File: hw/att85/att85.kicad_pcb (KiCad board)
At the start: 2 copper layers, 80 x 40 mm, 41 parts, among them J101 Barrel_Jack_Switch, J102 Screw_Terminal_01x03, J103 AVR-ISP-6, J104 Conn_01x02, Q101 BC817, SW101 SW_Push, SW102 SW_Push, SW103 SW_Push, SW104 SW_Push, SW105 SW_Push, SW106 SW_Push, U101 ATtiny85-20P, U102 MT3608-MODULE, U103 VS1838B

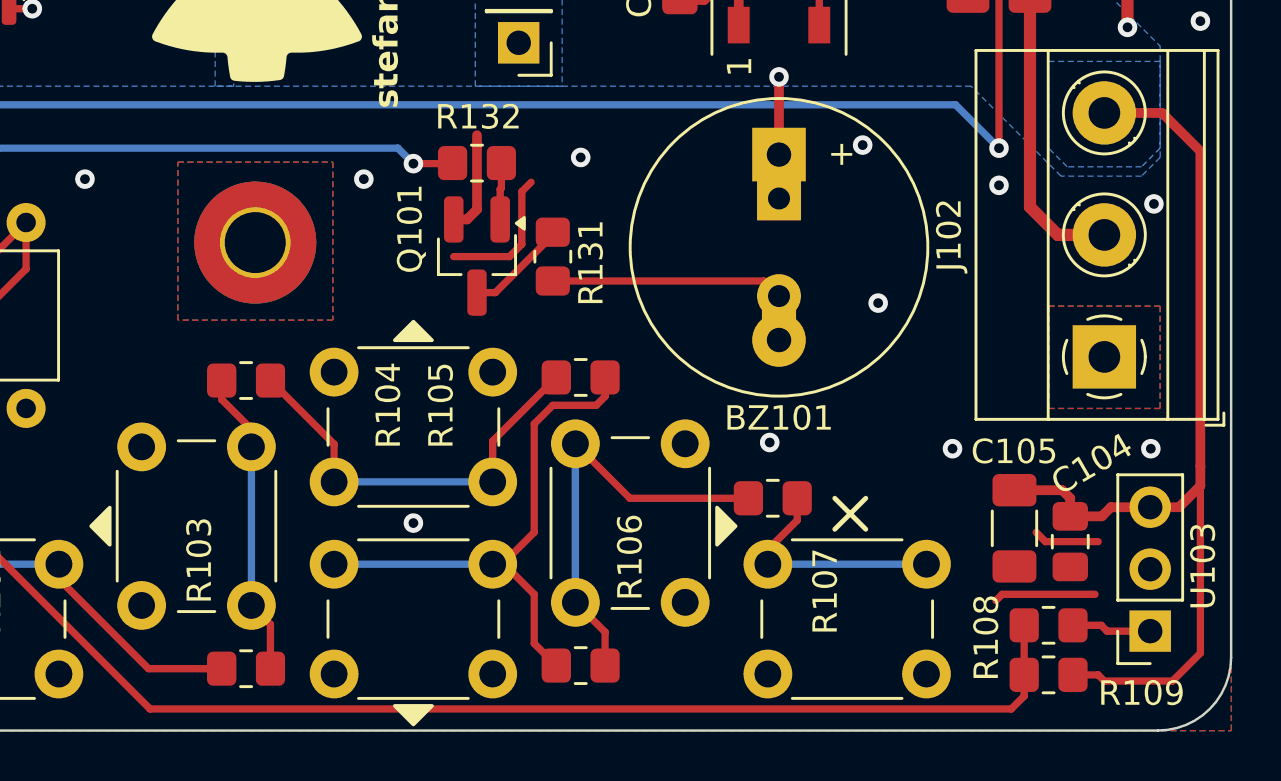
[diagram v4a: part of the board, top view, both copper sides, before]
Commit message: fix(hw): move IR receiver resistor according the datasheet
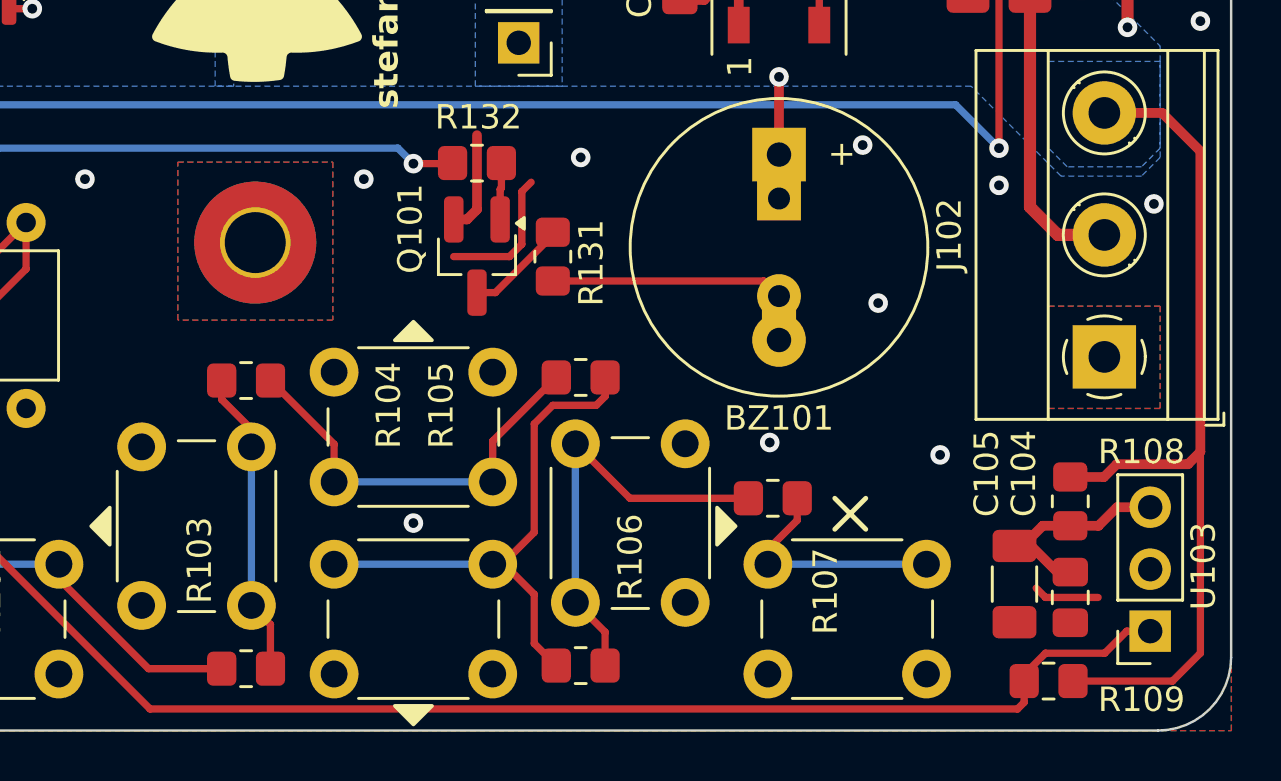
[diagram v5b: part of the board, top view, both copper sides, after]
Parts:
- moved R108 5.16 mm to (192.8, 105.5), turned to 90 degrees
- moved C104 2.29 mm to (192.8, 109.5)
- moved C105 2.29 mm to (190.5, 108.9)
- moved R109 0.25 mm to (191.9, 112.9)
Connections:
- C104 pad 1: +5V -> Net-(U103-VCC)
- C105 pad 1: +5V -> Net-(U103-VCC)
- R108 pad 1: /IR/MOSI -> Net-(U103-VCC)
- R108 pad 2: Net-(U103-OUT) -> +5V
- U103 pad 1: Net-(U103-OUT) -> /IR/MOSI
- U103 pad 3: +5V -> Net-(U103-VCC)
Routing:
- net Net-(U103-VCC): track 0.00 -> 8.95 mm
- net GND: track 27.6 -> 23.5 mm, vias 34 -> 33
- net +5V: track 90.5 -> 86.3 mm
- net /IR/MOSI: track 90.2 -> 94.3 mm
- net Net-(U103-OUT): track 3.26 -> 0.00 mm

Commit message: fix(hw): minor fixes
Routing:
- net +5V: track 86.3 -> 91.1 mm
- net Net-(U103-VCC): track 8.95 -> 8.13 mm

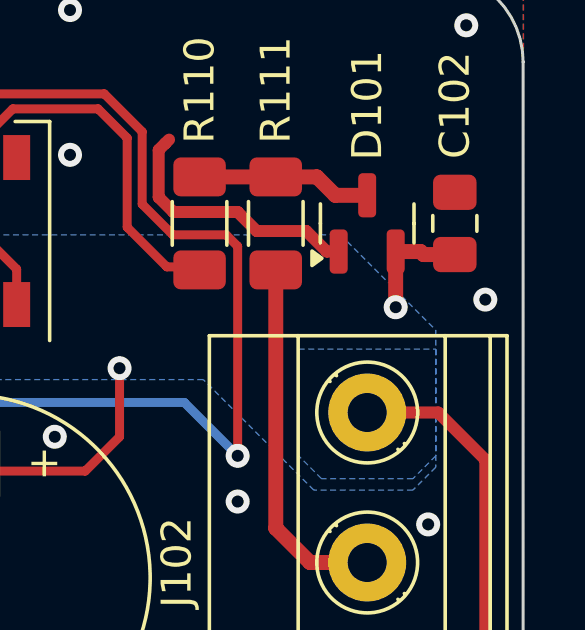
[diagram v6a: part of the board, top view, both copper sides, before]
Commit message: chore(hw): add cable connector identifiers
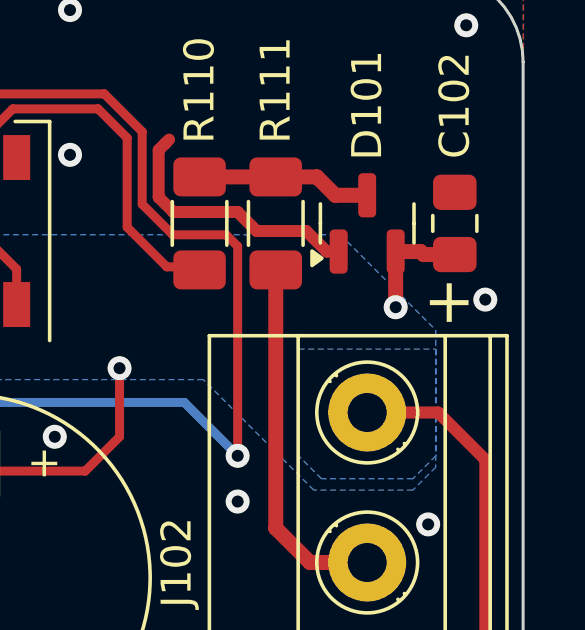
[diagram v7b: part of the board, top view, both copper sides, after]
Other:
- board text added: "+"
- board text added: "-"
- board text added: "D"
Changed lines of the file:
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@@
 		(layer "Edge.Cuts")
+	)
+	(gr_text "D"
+		(at 196.469 93.726 -90)
+		(layer "B.SilkS")
+		(effects
+			(font
+				(size 1.5 1.5)
+				(thickness 0.15)
+			)
+			(justify left bottom)
+		)
+	)
+	(gr_text "-"
+		(at 196.469 98.552 -90)
+		(layer "B.SilkS")
+		(effects
+			(font
+				(size 1.5 1.5)
+				(thickness 0.15)
+			)
+			(justify left bottom)
+		)
+	)
+	(gr_text "+"
+		(at 196.469 88.519 -90)
+		(layer "B.SilkS")
+		(effects
+			(font
+				(size 1.5 1.5)
+				(thickness 0.15)
+			)
+			(justify left bottom)
+		)
 	)
 	(gr_text "JLCJLCJLCJLC"
@@
 				(thickness 0.2)
 				(bold yes)
+			)
+			(justify left bottom)
+		)
+	)
+	(gr_text "+"
+		(at 196.088 85.09 270)
+		(layer "F.SilkS")
+		(effects
+			(font
+				(size 1.5 1.5)
+				(thickness 0.15)
 			)
 			(justify left bottom)
@@
 		)
 	)
+	(group ""
+		(members "2a1cfec7-b2ee-4269-ba18-3d75c5f62c1c" "a2b76c45-43ba-4265-ae5b-77250aec5f7a"
+			"affa7114-c58e-4877-910e-9fa9a47914d1"
+		)
+	)

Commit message: chore(hw): remove JLC PCB order number location (now on panel frame)
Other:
- board text removed: "JLCJLCJLCJLC"
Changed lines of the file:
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@@
-		)
-	)
-	(gr_text "JLCJLCJLCJLC"
-		(at 186.563 76.835 0)
-		(layer "B.SilkS")
-		(effects
-			(font
-				(size 1 1)
-				(thickness 0.15)
-			)
-			(justify right bottom mirror)
 		)
 	)
